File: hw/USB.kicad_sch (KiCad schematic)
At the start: 5 parts, among them J1 USB_C_Receptacle_USB2.0_14P

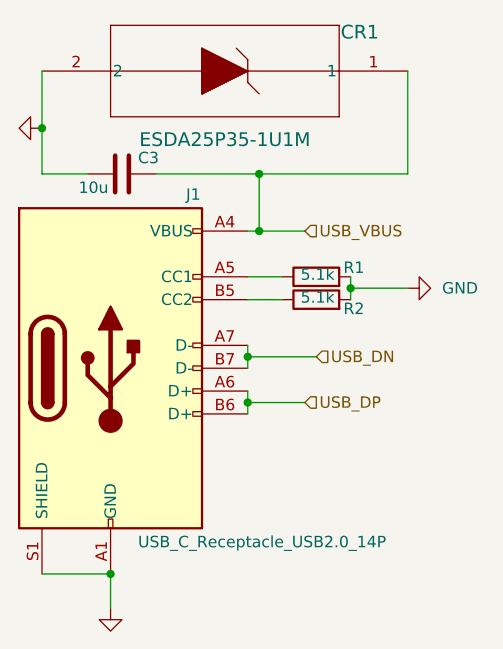
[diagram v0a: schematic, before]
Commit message: Work on footprinting and PCB
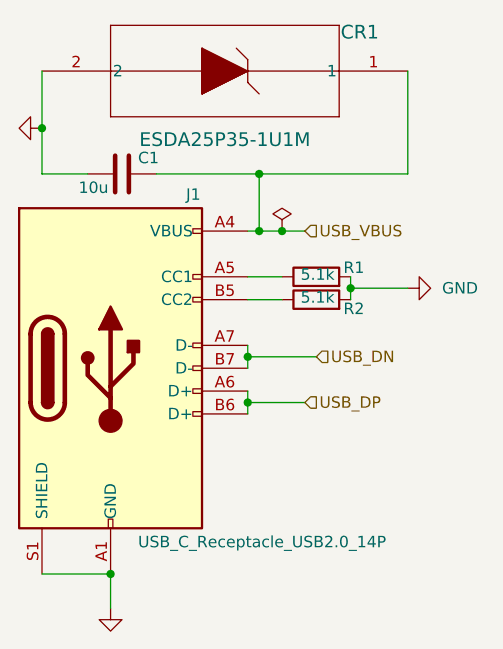
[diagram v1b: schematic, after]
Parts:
- C1: renamed from C3; footprint (none) -> Capacitor_SMD:C_0805_2012Metric
- CR1: footprint QFN1610_STM -> lib:QFN1610_STM-M
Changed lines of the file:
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@@
+	)
+	(junction
+		(at 64.77 68.58)
+		(diameter 0)
+		(color 0 0 0 0)
 	)
 	(junction
@@
 	(wire
 		(pts
+			(xy 64.77 68.58) (xy 67.31 68.58)
+		)
+		(stroke
+			(width 0)
+			(type default)
+		)
+	)
+	(wire
+		(pts
 			(xy 64.77 73.66) (xy 60.96 73.66)
 		)
@@
 	(wire
 		(pts
-			(xy 62.23 68.58) (xy 67.31 68.58)
+			(xy 62.23 68.58) (xy 64.77 68.58)
 		)
 		(stroke
@@
 	)
 	(symbol
+		(lib_id "power:PWR_FLAG")
+		(at 64.77 68.58 0)
+		(unit 1)
+		(exclude_from_sim no)
+		(in_bom yes)
+		(on_board yes)
+		(dnp no)
+		(fields_autoplaced yes)
+		(property "Reference" "#FLG2"
+			(at 64.77 66.675 0)
+			(effects
+				(font
+					(size 1.27 1.27)
+				)
+				(hide yes)
+			)
+		)
+		(property "Value" "PWR_FLAG"
+			(at 64.77 63.5 0)
+			(effects
+				(font
+					(size 1.27 1.27)
+				)
+				(hide yes)
+			)
+		)
+		(property "Footprint" ""
+			(at 64.77 68.58 0)
+			(effects
+				(font
+					(size 1.27 1.27)
+				)
+				(hide yes)
+			)
+		)
+		(property "Datasheet" "~"
+			(at 64.77 68.58 0)
+			(effects
+				(font
+					(size 1.27 1.27)
+				)
+				(hide yes)
+			)
+		)
+		(property "Description" "Special symbol for telling ERC where power comes from"
+			(at 64.77 68.58 0)
+			(effects
+				(font
+					(size 1.27 1.27)
+				)
+				(hide yes)
+			)
+		)
+		(pin "1"
+		)
+		(instances
+			(project ""
+				(path "/fdc0a18c-8dff-4a45-8df6-416fbc4de6f0/3f5409d7-86b0-49a5-819a-a592e97a9128"
+					(reference "#FLG2")
+					(unit 1)
+				)
+			)
+		)
+	)
+	(symbol
 		(lib_id "ESDA25P35:ESDA25P35-1U1M")
 		(at 78.74 50.8 180)
@@
 			)
 		)
-		(property "Footprint" "QFN1610_STM"
+		(property "Footprint" "lib:QFN1610_STM-M"
 			(at 78.74 50.8 0)
 			(effects
@@
 		(dnp no)
 		(fields_autoplaced yes)
-		(property "Reference" "#PWR02"
+		(property "Reference" "#PWR2"
 			(at 45.72 116.84 0)
 			(effects
@@
 			(project "Weltkatze"
 				(path "/fdc0a18c-8dff-4a45-8df6-416fbc4de6f0/3f5409d7-86b0-49a5-819a-a592e97a9128"
-					(reference "#PWR02")
+					(reference "#PWR2")
 					(unit 1)
 				)
@@
 		(on_board yes)
 		(dnp no)
-		(property "Reference" "C3"
+		(property "Reference" "C1"
 			(at 48.768 60.452 90)
 			(effects
@@
 			)
 		)
-		(property "Footprint" ""
+		(property "Footprint" "Capacitor_SMD:C_0805_2012Metric"
 			(at 43.18 63.1952 0)
 			(effects
@@
 			(project "Weltkatze"
 				(path "/fdc0a18c-8dff-4a45-8df6-416fbc4de6f0/3f5409d7-86b0-49a5-819a-a592e97a9128"
-					(reference "C3")
+					(reference "C1")
 					(unit 1)
 				)
@@
 		(dnp no)
 		(fields_autoplaced yes)
-		(property "Reference" "#PWR05"
+		(property "Reference" "#PWR3"
 			(at 85.09 74.93 0)
 			(effects
@@
 			(project "Weltkatze"
 				(path "/fdc0a18c-8dff-4a45-8df6-416fbc4de6f0/3f5409d7-86b0-49a5-819a-a592e97a9128"
-					(reference "#PWR05")
+					(reference "#PWR3")
 					(unit 1)
 				)
@@
 		(dnp no)
 		(fields_autoplaced yes)
-		(property "Reference" "#PWR01"
+		(property "Reference" "#PWR1"
 			(at 31.75 57.15 0)
 			(effects
@@
 			(project "Weltkatze"
 				(path "/fdc0a18c-8dff-4a45-8df6-416fbc4de6f0/3f5409d7-86b0-49a5-819a-a592e97a9128"
-					(reference "#PWR01")
+					(reference "#PWR1")
 					(unit 1)
 				)

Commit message: Footprinting, begin layout
I've assigned all the footprints except a few, so I've started on layout.
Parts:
- C1: footprint Capacitor_SMD:C_0805_2012Metric -> Capacitor_SMD:C_0603_1608Metric
- J1: footprint (none) -> Connector_USB:USB_C_Receptacle_HCTL_HC-TYPE-C-16P-01A
- R1, R2: footprint (none) -> Resistor_SMD:R_0603_1608Metric
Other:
- title: (none) -> Weltkatze
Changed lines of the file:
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@@
 	(generator_version "8.0")
 	(paper "A4")
+	(title_block
+		(title "Weltkatze")
+		(date "2025-02-25")
+		(rev "1")
+	)
 	(junction
 		(at 60.96 82.55)
@@
 			)
 		)
-		(property "Footprint" ""
+		(property "Footprint" "Connector_USB:USB_C_Receptacle_HCTL_HC-TYPE-C-16P-01A"
 			(at 49.53 83.82 0)
 			(effects
@@
 			)
 		)
-		(property "Footprint" ""
+		(property "Footprint" "Resistor_SMD:R_0603_1608Metric"
 			(at 68.58 77.978 90)
 			(effects
@@
 			)
 		)
-		(property "Footprint" "Capacitor_SMD:C_0805_2012Metric"
+		(property "Footprint" "Capacitor_SMD:C_0603_1608Metric"
 			(at 43.18 63.1952 0)
 			(effects
@@
 			)
 		)
-		(property "Footprint" ""
+		(property "Footprint" "Resistor_SMD:R_0603_1608Metric"
 			(at 68.58 75.438 90)
 			(effects

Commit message: Rest of the owl
Finish major layout, minor tweaks can be made
E.g. rotating the LEDs so they look pretty

Still need to make it so the inner PCB is manufacturable
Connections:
- net USB_DN renamed USBD_N
- net USB_DP renamed USBD_P
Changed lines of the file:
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@@
 		)
 	)
-	(hierarchical_label "USB_DN"
+	(hierarchical_label "USBD_N"
 		(shape input)
 		(at 68.58 82.55 0)
@@
 		)
 	)
-	(hierarchical_label "USB_DP"
+	(hierarchical_label "USBD_P"
 		(shape input)
 		(at 67.31 87.63 0)
@@
 		(dnp no)
 		(property "Reference" "J1"
-			(at 54.102 64.516 0)
+			(at 51.816 65.024 0)
 			(effects
 				(font

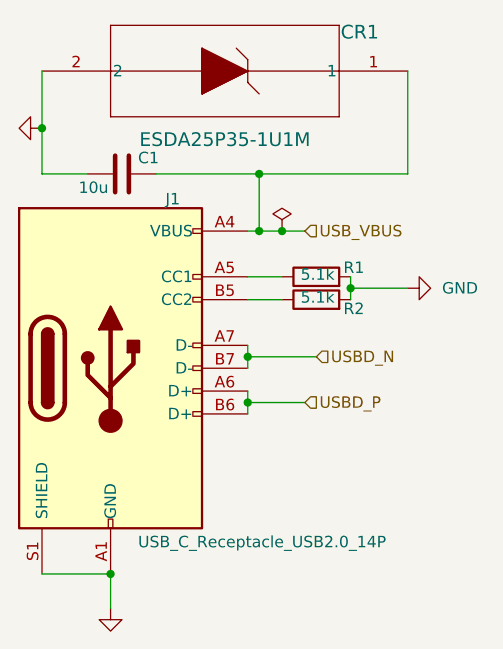
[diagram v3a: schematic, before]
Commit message: V1 REV1 Final!
I consider this design finished, as such I've submitted it to JLCPCB

I converted to a 6L pcb because its cheaper, in.3 and in.4 have no copper
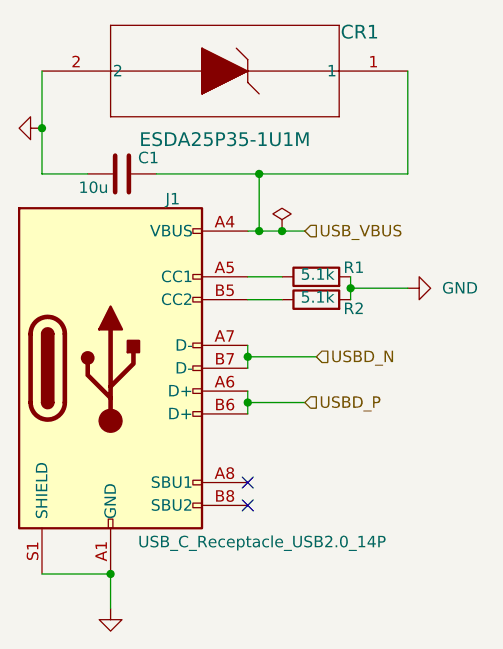
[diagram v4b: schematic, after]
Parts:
- J1: symbol Connector:USB_C_Receptacle_USB2.0_14P -> Connector:USB_C_Receptacle_USB2.0_16P
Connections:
- no-connect marks 0 -> 2
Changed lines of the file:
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@@
 		(color 0 0 0 0)
+	)
+	(no_connect
+		(at 60.96 99.06)
+	)
+	(no_connect
+		(at 60.96 96.52)
 	)
 	(wire
@@
 	)
 	(symbol
-		(lib_id "Connector:USB_C_Receptacle_USB2.0_14P")
+		(lib_id "Connector:USB_C_Receptacle_USB2.0_16P")
 		(at 45.72 83.82 0)
 		(unit 1)
@@
 			)
 		)
-		(property "Description" "USB 2.0-only 14P Type-C Receptacle connector"
+		(property "Description" "USB 2.0-only 16P Type-C Receptacle connector"
 			(at 45.72 83.82 0)
 			(effects
@@
 		(pin "B7"
 		)
+		(pin "A8"
+		)
+		(pin "B8"
+		)
 		(instances

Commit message: Update to kicad v9
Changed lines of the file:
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@@
 (kicad_sch
-	(version 20231120)
+	(version 20250114)
 	(generator "eeschema")
-	(generator_version "8.0")
+	(generator_version "9.0")
 	(paper "A4")
 	(title_block
